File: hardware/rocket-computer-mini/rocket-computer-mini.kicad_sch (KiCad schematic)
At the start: 8 parts

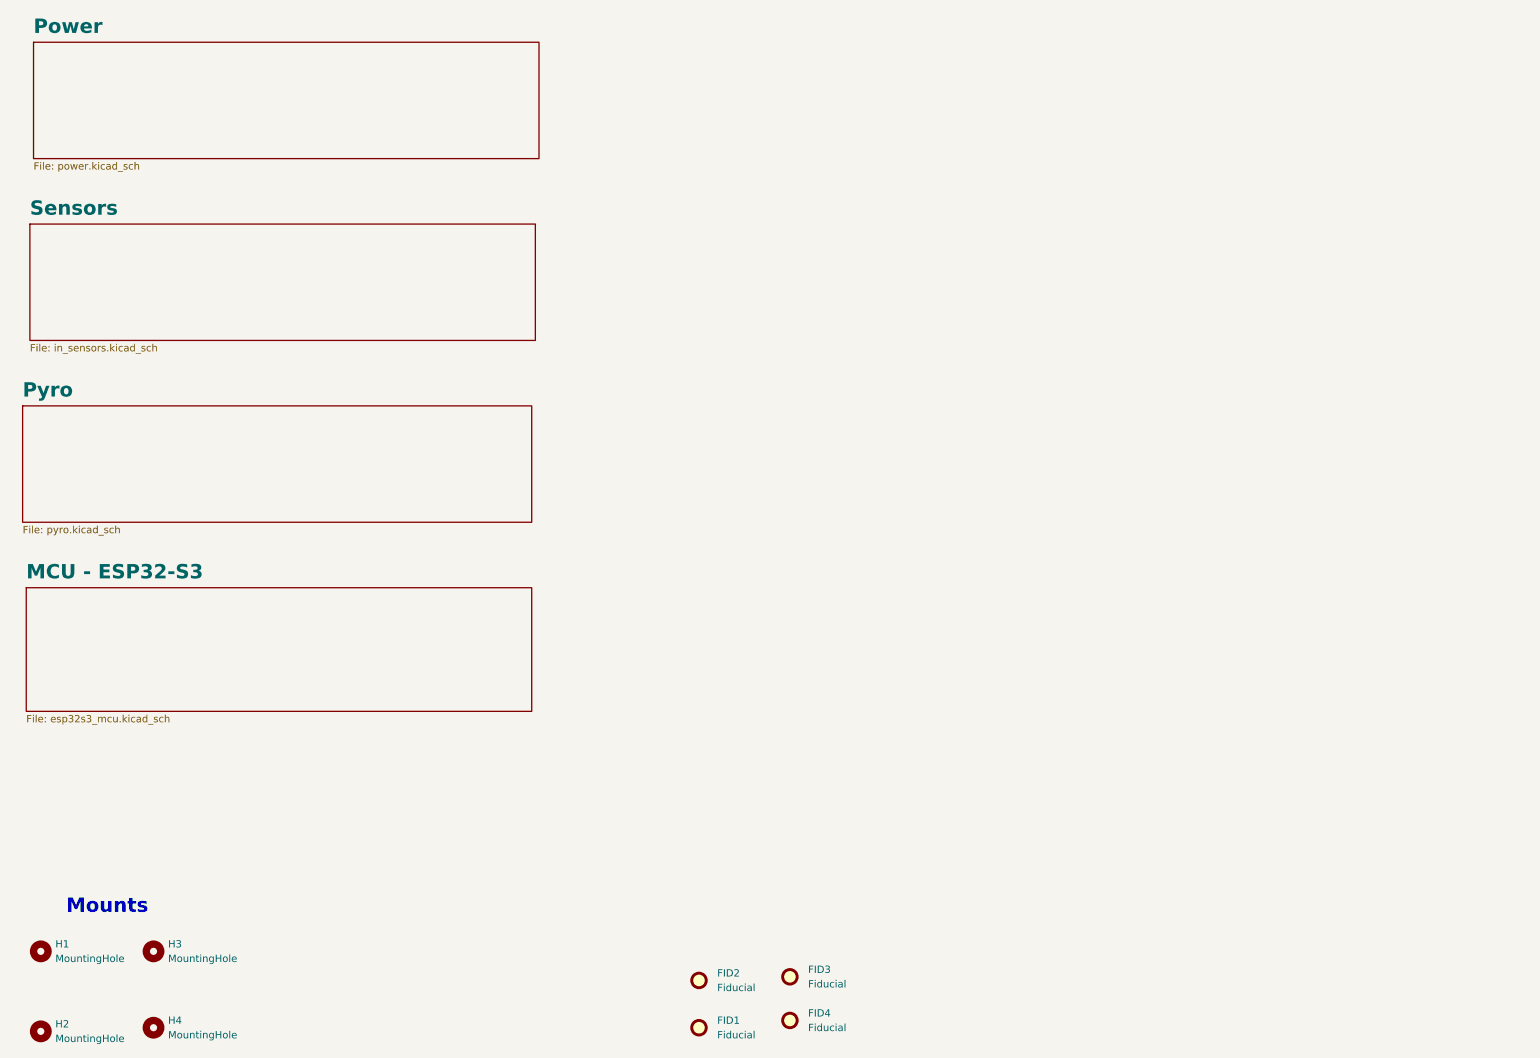
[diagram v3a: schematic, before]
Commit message: hardware(rocket-computer-mini): second ESP32-S3 as the flight computer
Adds an ESP32-S3RH2 back as a dedicated flight computer, restoring
rocket-computer's two-processor split with an S3 on both ends instead of
an S3 and a P4. Schematic only -- the PCB is untouched.

New sheet fc_esp32s3.kicad_sch ("MCU - ESP32-S3 Flight Computer") is a
copy of the out-computer sheet with the 2.4 GHz chip antenna, its
matching network and the NAND removed. U32 keeps its own boot flash
(U33), both crystals, the boot button, the strapping network and the
full decoupling set, in a C110/R110 block so the sheet is identifiable
in the BOM. Its supplies come off V_MCU_SWTCH, not +3V3.

The flight computer starts off and holds itself on. D9 (BAV170M)
OR-gates FC_EN_OC (OC GPIO7) with FC_EN_HOLD (FC GPIO3) into
POWER_SWITCH -> U30 EN/UVLO, with R84 holding the rail off at power-on
and C105 riding out a brief drop-out. The out computer boots on the
always-on rail and starts the flight computer, which then holds its own
rail up, so an out-computer reboot in flight cannot power it down. This
is rocket-computer's arrangement reproduced part for part.

All four pyro channels and PYRO_ARM move to the flight computer, along
with the IMU/baro SPI, both interrupts and the GNSS UART -- each on the
same GPIO it already had, so pin-budget.md's assignment carries over
unchanged and simply belongs to U32 now. The out computer keeps the LoRa
radio, the chip antenna, the memory bus, the power-monitor I2C and USB,
and gains twelve spare pads.

The link is six wires with rocket-computer's net names and protocols:
I2S (ESP_SCLK/ESP_CS/ESP_SDO/ESP_SDI) plus I2C (ESP_SCL/ESP_SDA), pulled
up by R115/R116 to V_MCU_SWTCH. The out computer's six GPIO numbers are
identical to rocket-computer's, so projects/out_computer ports with a
board header alone. The flight computer matches on I2S BCLK (21) and WS
(18) but not the data pair -- rocket-computer's P4 uses GPIO19/20, which
on an S3 are the USB D-/D+ pads and are spe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
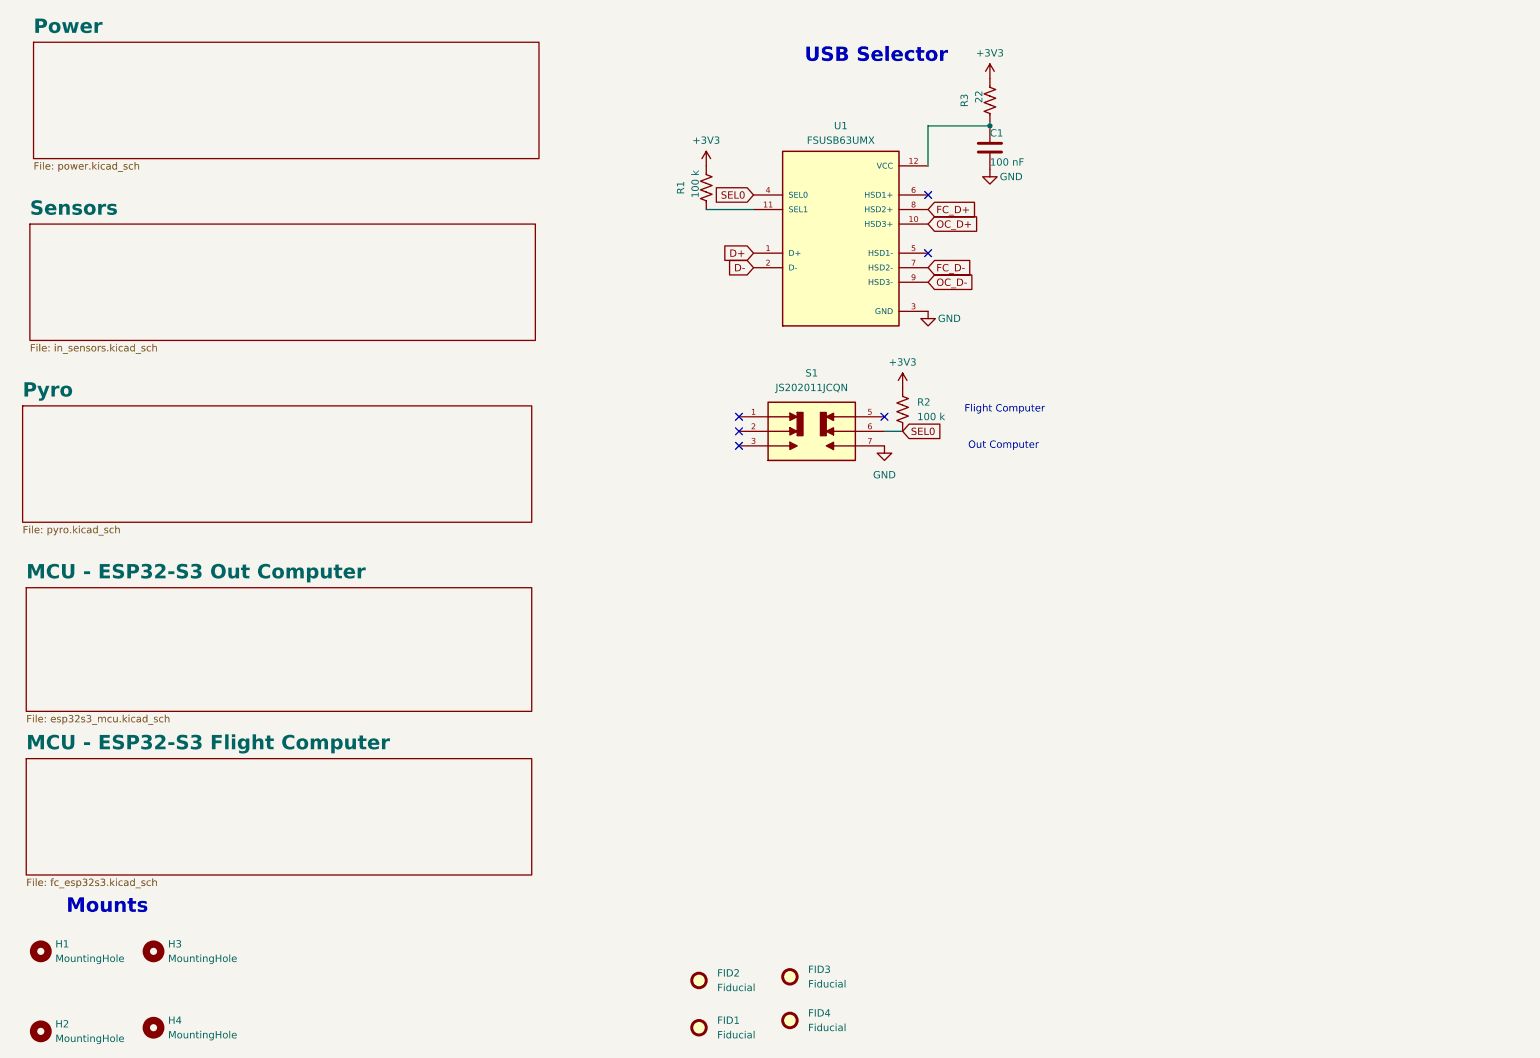
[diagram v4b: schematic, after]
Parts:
- added C1: 100 nF, Capacitor_SMD:C_0402_1005Metric, symbol Device:C
- added R1, R2: 100 k, Resistor_SMD:R_0402_1005Metric, symbol Device:R_US
- added R3: 22, Resistor_SMD:R_0402_1005Metric, symbol Device:R_US
- added S1: JS202011JCQN, Footprints:SW_JS202011JCQN, symbol Custom:JS202011JCQN
- added U1: FSUSB63UMX, Footprints:QFN40P180X180X55-12N, symbol Custom:FSUSB63UMX
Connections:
- new net: R1.1, U1.11 (SEL1)
- new net: C1.1, R3.1, U1.12 (VCC)
- new net +3V3: R1.2, R2.2, R3.2
- new net D+: U1.1 (D+)
- new net D-: U1.2 (D-)
- new net FC_D+: U1.8 (HSD2+)
- new net FC_D-: U1.7 (HSD2-)
- new net GND: C1.2, S1.7, U1.3 (GND)
- new net OC_D+: U1.10 (HSD3+)
- new net OC_D-: U1.9 (HSD3-)
- new net SEL0: R2.1, S1.6, U1.4 (SEL0)
- no-connect marks 0 -> 6
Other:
- sheet MCU - ESP32-S3 renamed MCU - ESP32-S3 Out Computer
- added sheet MCU - ESP32-S3 Flight Computer (fc_esp32s3.kicad_sch)
- note added: "Flight Computer"
- note added: "Out Computer"
- note added: "USB Selector"

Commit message: rocket-computer-mini: the same ERC pass — 33 errors to 10, the ten being spare pads left unflagged on purpose (#1371)
The mini carried 33 ERC errors after the shared-symbol fixes of #1367: 24
unflagged pins, six power inputs on nets with no power output, two ground
pins typed as power outputs arguing with each other, and one input the
symbol said nobody drives. None was electrical. The netlist is byte-identical
before and after on every board touched.

QMC5883P and BMP581 grounds become power inputs (library + cache). The
reverse-battery FET's pins become passive on both rocket computers — a
MOSFET gate typed bidirectional warned against every ground driver.
TPS259631DDAR joins the library; it lived only in the mini's cache. Seven
PWR_FLAGs: GND, VBAT_CON, V_BUCK, VBUS, U1 VCC, both VDD3P3 nets. Fourteen
no-connect flags on pins both reviews cleared: the octal-SPI pads of both
processors, the GNSS reset / external-antenna / antenna-detect pads, the
IMU's INT2, the radio's DIO3, the INA230 ALERT, the USB-C sideband pair.

The ten that remain are the out computer's spare GPIO pads. The README's
open-items list says they stay unflagged so nobody reads them as
permanently unused; that decision is respected, and the README's status
section now records the floor and what it consists of.

Mini 33 -> 10 errors, warnings 783 -> 785 (four off-grid endpoints inherited
from the half-grid hold-up block and eFuse placement, minus the two fixed).
V10 unchanged at 0 errors, one warning fewer. Base-station and LoRa boards
untouched.

Co-authored-by: Claude Fable 5.1 <noreply@anthropic.com>
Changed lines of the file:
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@@
 	(wire
 		(pts
-			(xy 183.515 35.56) (xy 172.72 35.56)
+			(xy 183.515 35.56) (xy 177.8 35.56)
+		)
+		(stroke
+			(width 0)
+			(type default)
+		)
+	)
+	(wire
+		(pts
+			(xy 177.8 35.56) (xy 172.72 35.56)
 		)
 		(stroke
@@
 	)
 	(embedded_fonts no)
+	(junction
+		(at 177.8 35.56)
+		(diameter 0)
+		(color 0 0 0 0)
+	)
+	(symbol
+		(lib_id "power:PWR_FLAG")
+		(at 177.8 35.56 0)
+		(unit 1)
+		(body_style 1)
+		(exclude_from_sim no)
+		(in_bom yes)
+		(on_board yes)
+		(in_pos_files yes)
+		(dnp no)
+		(property "Reference" "#FLG01"
+			(at 177.8 33.655 0)
+			(hide yes)
+			(show_name no)
+			(do_not_autoplace no)
+			(effects
+				(font
+					(size 1.27 1.27)
+				)
+			)
+		)
+		(property "Value" "PWR_FLAG"
+			(at 175.895 33.655 0)
+			(show_name no)
+			(do_not_autoplace no)
+			(effects
+				(font
+					(size 1.27 1.27)
+				)
+				(justify right)
+			)
+		)
+		(property "Footprint" ""
+			(at 177.8 35.56 0)
+			(hide yes)
+			(show_name no)
+			(do_not_autoplace no)
+			(effects
+				(font
+					(size 1.27 1.27)
+				)
+			)
+		)
+		(property "Datasheet" ""
+			(at 177.8 35.56 0)
+			(hide yes)
+			(show_name no)
+			(do_not_autoplace no)
+			(effects
+				(font
+					(size 1.27 1.27)
+				)
+			)
+		)
+		(property "Description" "Special symbol for telling ERC where power comes from"
+			(at 177.8 35.56 0)
+			(hide yes)
+			(show_name no)
+			(do_not_autoplace no)
+			(effects
+				(font
+					(size 1.27 1.27)
+				)
+			)
+		)
+		(pin "1"
+		)
+		(instances
+			(project "rocket-computer-mini"
+				(path "/ae61c2c4-72e9-4776-93ae-2e716b9dc70f"
+					(reference "#FLG01")
+					(unit 1)
+				)
+			)
+		)
+	)
 )

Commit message: hardware(mini): #1030 hygiene — the pyro P-FETs and the NAND get symbols named for the fitted parts, stale cached copies are refreshed, every sheet has a title block; netlist unchanged
What the owner's 2026-09-11 status on #1030 left open, and what this does:

Borrowed symbols. U6/U7/U8/U10 (WSD20L50DN33) were drawn with the V10's
TPN4R712MD box symbol and U11 (GD5F1GQ5UEYIGR) with the MX35UF4G24AD-Z4I8
symbol. Custom.kicad_sym gains WSD20L50DN33 (the same 8-pin box, pins
typed passive instead of unspecified, a description) and GD5F1GQ5UEYIGR
(the same WSON-8 pinout, CS# typed input, the pad passive); the five
instances point at them. Pin numbers and names are unchanged, so every
net and every pinfunction in the exported netlist is identical to the
pre-edit export; only the libsource part names of those five differ.
The V10 keeps its own symbols untouched.

Cached copies. Eighteen cached symbols differed from the shared library
only by a footprint-library nickname ("TPS2121RUXR:IC_..." vs
"Footprints:IC_...", a fork-era artefact) or a datasheet/description
line; each was replaced by the library copy after a normalised diff
proved that was the whole difference. Cached copies that differ in
pins or graphics (U30's TPS22810DRVR_1 variant, the LC86G, the QMC5883P,
the hold-up converter and others) are deliberately not touched: a
refresh there could move a pin end off its wire.

Title blocks. None of the six sheets had one (nor do the V10's — only
the GNSS carrier's did). Each now carries title, date 2026-09-05 (the
V1.0.1 release the print corresponds to), rev V1 and company, in the
carrier's format.

ARM_GATE. The label has been back since 2026-09-02 as a sheet-local
label; its net is /Pyro/ARM_GATE, which is KiCad's naming for a local
net in a sub-sheet, not a lost label. The README now says so.

Measured: ERC --severity-all 795 -> 737 (10 errors unchanged, all the
out computer's bare spare pads; 704 off-grid unchanged; pin_to_pin
56 -> 22; lib_symbol_mismatch 25 -> 1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
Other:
- company: (none) -> TinkerRocket
- title: (none) -> rocket-computer-mini
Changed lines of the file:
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@@
 	(generator_version "10.0")
 	(paper "A4")
+	(title_block
+		(title "rocket-computer-mini")
+		(date "2026-09-05")
+		(rev "V1")
+		(company "TinkerRocket")
+	)
 	(text "USB Selector"
 		(exclude_from_sim no)
